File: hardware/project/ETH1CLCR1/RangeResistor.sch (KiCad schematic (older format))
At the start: 13 parts

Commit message: Schematic design
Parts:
- added C? (x5): C, symbol Device:C
- added C? (x2): 10p, symbol Device:C
- added C?: 2-8p, symbol Device:CTRIM
- added C?: 5-35p, symbol Device:CTRIM
- added C?: 1u, symbol Device:C
- added D? (x5): 1N4148, symbol Device:D
- added D? (x2): D, symbol Device:D
- added J? (x2): Conn_Coaxial, symbol Connector:Conn_Coaxial
- added K?: TQ2SA-5V, symbol ETH1CLCR1:TQ2SA-5V
- added Q? (x2): BC847W, Package_TO_SOT_SMD:SOT-323_SC-70, symbol Transistor_BJT:BC847W
- added Q?: 2N2218A, symbol Device:Q_NPN_BEC
- added Q?: 2N2904A, symbol Device:Q_PNP_BEC
- added R? (x20): R, symbol Device:R
- added R?: 10, symbol Device:R
- added R?: 100, symbol Device:R
- added R?: 1k01, symbol Device:R
- added R? (x6): 10k, symbol Device:R
- added R? (x2): 47, symbol Device:R
- added R? (x2): 51R1, symbol Device:R
- added R? (x2): 2R7/2W, symbol Device:R
- added R? (x2): 261, symbol Device:R
- added R?: 90k, symbol Device:R
- added RV?: 500, symbol Device:R_POT_TRIM
- added U? (x12): TLP3542, Package_DIP:DIP-5-6_W7.62mm, symbol Relay_SolidState:TLP3542
- added U?: HA3-2525-5Z, symbol ETH1CLCR1:HA3-2525-5Z
- added U? (x3): RC4558, symbol Amplifier_Operational:RC4558
- added U?: AD5293BRUZ-20, Package_SO:TSSOP-14_4.4x5mm_P0.65mm, symbol Potentiometer_Digital:AD5293
- D? (x4): value D_Small -> 1N4148
- R?: value R -> 100
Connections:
- net labels added: +15VF, +3.3VP, +5VF, -15VF, 100KNPN, Err, Lc, Lp, R100CRT, R100KCRT, R10CRT, R10KCRT, R1KCRT
- wire segments 37 -> 241
- no-connect marks 0 -> 4
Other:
- note removed: "Protection circuit"
- moved on the sheet: C?, D?, R?

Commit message: Schematic design
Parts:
- gave numbers to parts that had none: 91
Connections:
- net labels added: +12VF, -12VF

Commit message: Schematic design
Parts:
- removed D1305, D1306: D_Small, symbol Device:D_Small
- removed J1301, J1302: Conn_Coaxial, symbol Connector:Conn_Coaxial
- removed U1302, U1305, U1306, U1307, U1308, U1309, U1310, U1311, U1312, U1313, U1314, U1315: TLP3542, Package_DIP:DIP-5-6_W7.62mm, symbol Relay_SolidState:TLP3542
- added D1305: BAT54SW, Package_TO_SOT_SMD:SOT-323_SC-70, symbol Diode:BAT54SW
- added RV1302: 20k, Resistor_SMD:R_0603_1608Metric_Pad1.05x0.95mm_HandSolder, symbol Device:R_POT_TRIM
- added U1302, U1305, U1306, U1307, U1308, U1309, U1310, U1311, U1312, U1313, U1314, U1315: AQY212GS, symbol ETH1CLCR1:AQY212GS
- C1302, C1303, C1311, C1312: footprint (none) -> Capacitor_SMD:C_0603_1608Metric_Pad1.05x0.95mm_HandSolder
- C1304: value C -> 1u
- C1305: value C -> 47p; footprint (none) -> Capacitor_SMD:C_0603_1608Metric_Pad1.05x0.95mm_HandSolder
- C1307: value C -> 33p; footprint (none) -> Capacitor_SMD:C_0603_1608Metric_Pad1.05x0.95mm_HandSolder
- C1308: value C -> 6800p; footprint (none) -> Capacitor_SMD:C_0603_1608Metric_Pad1.05x0.95mm_HandSolder
- C1309: value C -> 39p; footprint (none) -> Capacitor_SMD:C_0603_1608Metric_Pad1.05x0.95mm_HandSolder
- D1307, D1308: value D -> 1N4148
- R1302: value R -> 1k
- R1303, R1304, R1305, R1306, R1309, R1310, R1311, R1314, R1315, R1316, R1317, R1319, R1322, R1323, R1325, R1326, R1327, R1329, R1340, R1343, RV1301: footprint (none) -> Resistor_SMD:R_0603_1608Metric_Pad1.05x0.95mm_HandSolder
- R1307, R1330, R1331, R1332, R1333, R1334, R1335, R1336, R1337, R1339, R1341, R1342: value R -> 330; footprint (none) -> Resistor_SMD:R_0603_1608Metric_Pad1.05x0.95mm_HandSolder
- R1308: value R -> 550; footprint (none) -> Resistor_SMD:R_0603_1608Metric_Pad1.05x0.95mm_HandSolder
- R1312, R1324: value R -> 10k; footprint (none) -> Resistor_SMD:R_0603_1608Metric_Pad1.05x0.95mm_HandSolder
- R1313: value R -> 5M6; footprint (none) -> Resistor_SMD:R_0603_1608Metric_Pad1.05x0.95mm_HandSolder
- R1318: value R -> 3k3; footprint (none) -> Resistor_SMD:R_0603_1608Metric_Pad1.05x0.95mm_HandSolder
- R1328: value R -> 1k111; footprint (none) -> Resistor_SMD:R_0603_1608Metric_Pad1.05x0.95mm_HandSolder
- R1338: value R -> 13R3; footprint (none) -> Resistor_SMD:R_0603_1608Metric_Pad1.05x0.95mm_HandSolder
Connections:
- net labels added: +3.3VF, HA3-COMP, HPOT, LCUR, LPOT, RELAY_CTR, RR_CLK, RR_OFFS1, RR_RDY, RR_SDI, RR_SDO, RR_~CS, RR_~RST
- net labels removed: +3.3VP, Lc, Lp
- wire segments 241 -> 242
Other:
- moved on the sheet: C1312, Q1304, R1305, R1343, U1304C

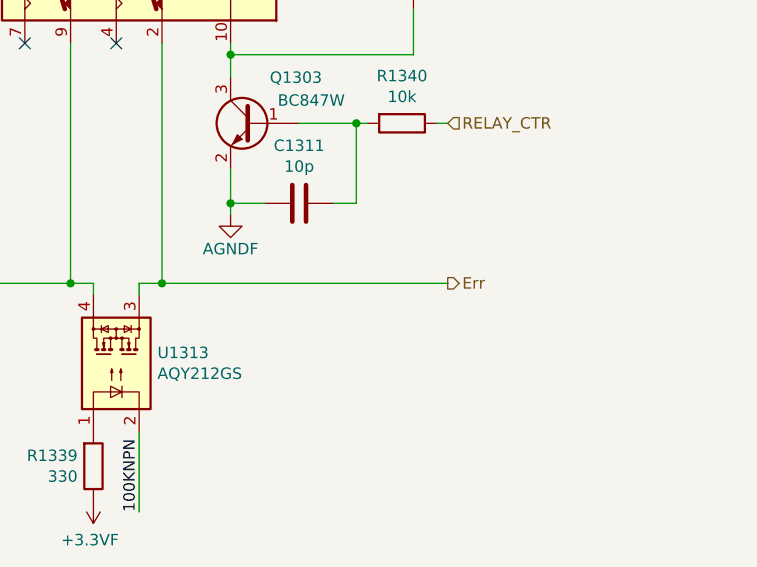
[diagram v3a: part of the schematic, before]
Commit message: Need to redesign the AC source, the LT1468 is too slow.
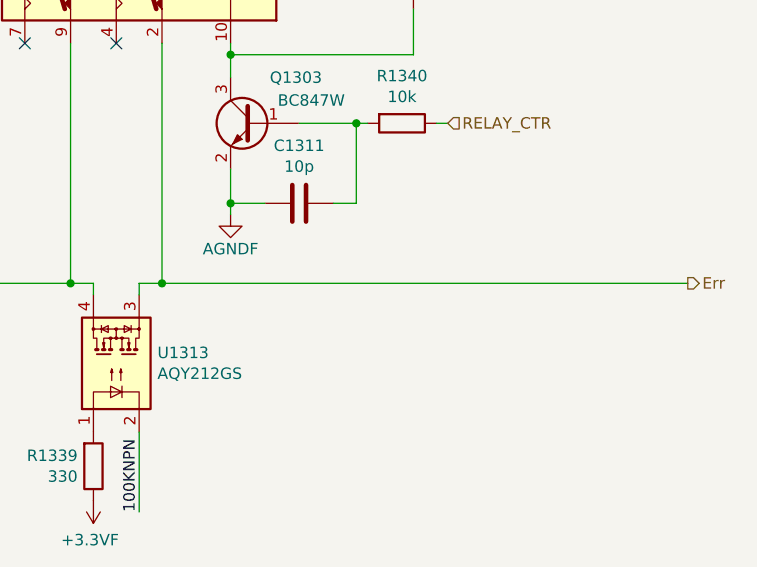
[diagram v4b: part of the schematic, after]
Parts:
- D1301, D1302, D1303, D1304, D1307, D1308, D1309, D1310, D1311, D1312, D1313: footprint (none) -> Diode_SMD:D_SOD-123
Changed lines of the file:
@@
 F 0 "D1313" V 13104 6579 50  0000 L CNN
 F 1 "1N4148" V 13195 6579 50  0000 L CNN
-F 2 "" H 13150 6500 50  0001 C CNN
+F 2 "Diode_SMD:D_SOD-123" H 13150 6500 50  0001 C CNN
 F 3 "~" H 13150 6500 50  0001 C CNN
 	1    13150 6500
@@
 Connection ~ 11650 7850
 Wire Wire Line
-	12050 7850 13300 7850
+	12050 7850 14350 7850
 Connection ~ 12050 7850
-Text HLabel 13300 7850 2    50   Output ~ 0
+Text HLabel 14350 7850 2    50   Output ~ 0
 Err
 $Comp
@@
 F 0 "D1310" H 7900 8034 50  0000 C CNN
 F 1 "1N4148" H 7900 8125 50  0000 C CNN
-F 2 "" H 7900 8250 50  0001 C CNN
+F 2 "Diode_SMD:D_SOD-123" H 7900 8250 50  0001 C CNN
 F 3 "~" H 7900 8250 50  0001 C CNN
 	1    7900 8250
@@
 F 0 "D1309" H 7900 7666 50  0000 C CNN
 F 1 "1N4148" H 7900 7575 50  0000 C CNN
-F 2 "" H 7900 7450 50  0001 C CNN
+F 2 "Diode_SMD:D_SOD-123" H 7900 7450 50  0001 C CNN
 F 3 "~" H 7900 7450 50  0001 C CNN
 	1    7900 7450
@@
 F 0 "D1308" V 7346 8271 50  0000 R CNN
 F 1 "1N4148" V 7255 8271 50  0000 R CNN
-F 2 "" H 7300 8350 50  0001 C CNN
+F 2 "Diode_SMD:D_SOD-123" H 7300 8350 50  0001 C CNN
 F 3 "~" H 7300 8350 50  0001 C CNN
 	1    7300 8350
@@
 F 0 "D1307" V 7346 7271 50  0000 R CNN
 F 1 "1N4148" V 7255 7271 50  0000 R CNN
-F 2 "" H 7300 7350 50  0001 C CNN
+F 2 "Diode_SMD:D_SOD-123" H 7300 7350 50  0001 C CNN
 F 3 "~" H 7300 7350 50  0001 C CNN
 	1    7300 7350
@@
 F 0 "D1304" V 3596 7532 50  0000 R CNN
 F 1 "1N4148" V 3505 7532 50  0000 R CNN
-F 2 "" V 3550 7600 50  0001 C CNN
+F 2 "Diode_SMD:D_SOD-123" V 3550 7600 50  0001 C CNN
 F 3 "~" V 3550 7600 50  0001 C CNN
 	1    3550 7600
@@
 F 0 "D1302" V 3004 7668 50  0000 L CNN
 F 1 "1N4148" V 3095 7668 50  0000 L CNN
-F 2 "" V 3050 7600 50  0001 C CNN
+F 2 "Diode_SMD:D_SOD-123" V 3050 7600 50  0001 C CNN
 F 3 "~" V 3050 7600 50  0001 C CNN
 	1    3050 7600
@@
 F 0 "D1303" V 3596 6432 50  0000 R CNN
 F 1 "1N4148" V 3505 6432 50  0000 R CNN
-F 2 "" V 3550 6500 50  0001 C CNN
+F 2 "Diode_SMD:D_SOD-123" V 3550 6500 50  0001 C CNN
 F 3 "~" V 3550 6500 50  0001 C CNN
 	1    3550 6500
@@
 F 0 "D1301" V 3004 6568 50  0000 L CNN
 F 1 "1N4148" V 3095 6568 50  0000 L CNN
-F 2 "" V 3050 6500 50  0001 C CNN
+F 2 "Diode_SMD:D_SOD-123" V 3050 6500 50  0001 C CNN
 F 3 "~" V 3050 6500 50  0001 C CNN
 	1    3050 6500
@@
 F 0 "D1311" H 8300 7666 50  0000 C CNN
 F 1 "1N4148" H 8300 7575 50  0000 C CNN
-F 2 "" H 8300 7450 50  0001 C CNN
+F 2 "Diode_SMD:D_SOD-123" H 8300 7450 50  0001 C CNN
 F 3 "~" H 8300 7450 50  0001 C CNN
 	1    8300 7450
@@
 F 0 "D1312" H 8300 8034 50  0000 C CNN
 F 1 "1N4148" H 8300 8125 50  0000 C CNN
-F 2 "" H 8300 8250 50  0001 C CNN
+F 2 "Diode_SMD:D_SOD-123" H 8300 8250 50  0001 C CNN
 F 3 "~" H 8300 8250 50  0001 C CNN
 	1    8300 8250

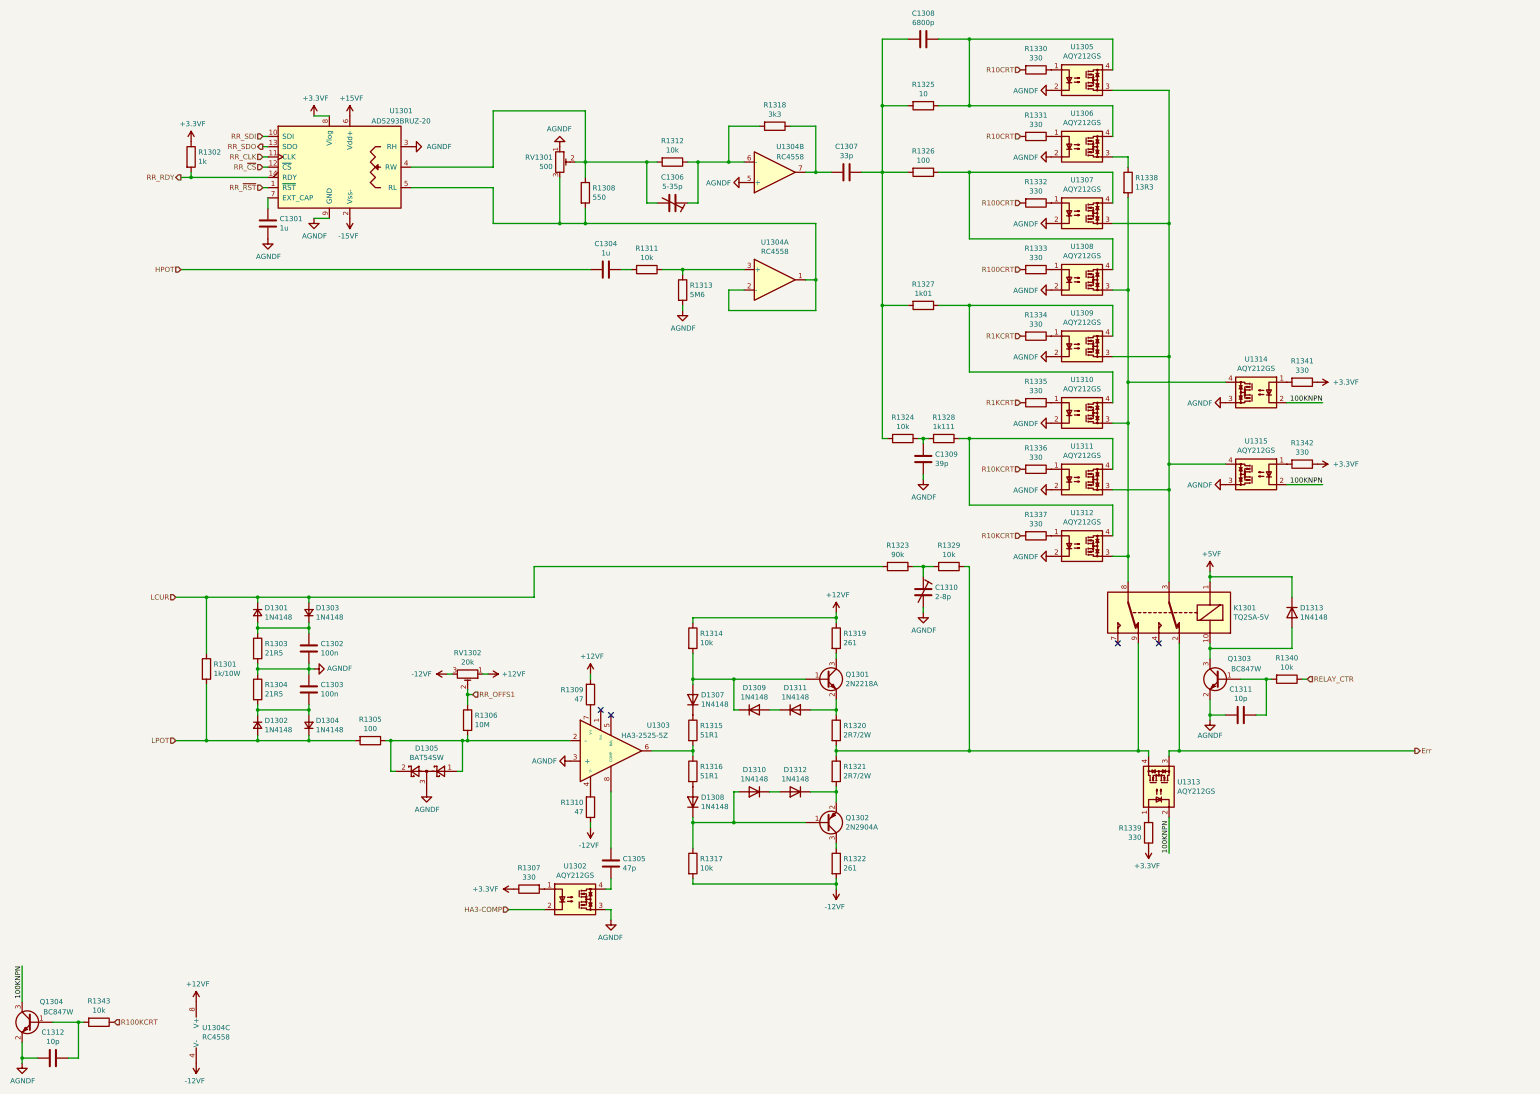
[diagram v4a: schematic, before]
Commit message: Footprint asigment (not finished).
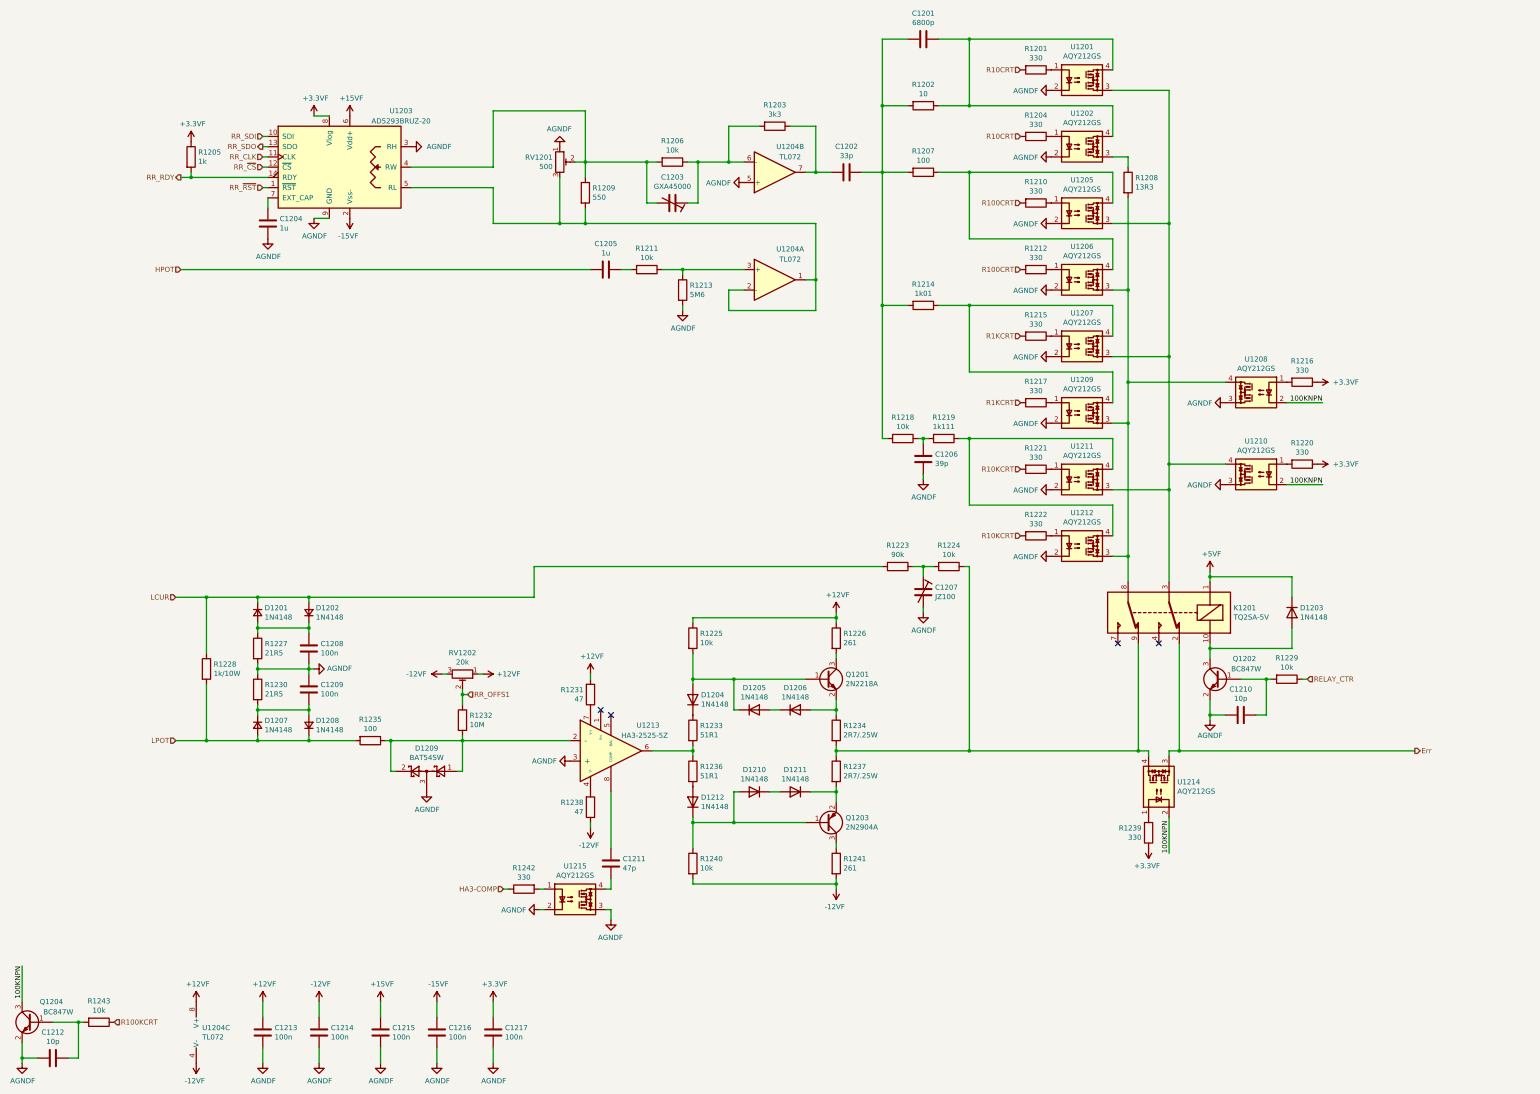
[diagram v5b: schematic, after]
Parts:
- removed U1304: RC4558, symbol Amplifier_Operational:RC4558
- added C1213, C1214, C1215, C1216, C1217: 100n, Capacitor_SMD:C_0603_1608Metric_Pad1.05x0.95mm_HandSolder, symbol Device:C
- added U1204: TL072, Package_SO:SOIC-8_3.9x4.9mm_P1.27mm, symbol Amplifier_Operational:TL072
- C1203: renamed from C1306; value 5-35p -> GXA45000
- C1204: renamed from C1301; footprint (none) -> Capacitor_SMD:C_0805_2012Metric_Pad1.15x1.40mm_HandSolder
- C1205: renamed from C1304; footprint (none) -> Capacitor_SMD:C_0805_2012Metric_Pad1.15x1.40mm_HandSolder
- C1207: renamed from C1310; value 2-8p -> JZ100
- K1201: renamed from K1301; footprint (none) -> ETH1CLCR1:SA
- Q1201: renamed from Q1301; footprint (none) -> Package_TO_SOT_THT:TO-39-3
- Q1203: renamed from Q1302; footprint (none) -> Package_TO_SOT_THT:TO-39-3
- R1205: renamed from R1302; footprint (none) -> Resistor_SMD:R_0603_1608Metric_Pad1.05x0.95mm_HandSolder
- R1234: renamed from R1320; value 2R7/2W -> 2R7/.25W
- R1237: renamed from R1321; value 2R7/2W -> 2R7/.25W
- U1201: renamed from U1305; footprint (none) -> ETH1CLCR1:AQY212GS
- U1202: renamed from U1306; footprint (none) -> ETH1CLCR1:AQY212GS
- U1205: renamed from U1307; footprint (none) -> ETH1CLCR1:AQY212GS
- U1206: renamed from U1308; footprint (none) -> ETH1CLCR1:AQY212GS
- U1207: renamed from U1309; footprint (none) -> ETH1CLCR1:AQY212GS
- U1208: renamed from U1314; footprint (none) -> ETH1CLCR1:AQY212GS
- U1209: renamed from U1310; footprint (none) -> ETH1CLCR1:AQY212GS
- U1210: renamed from U1315; footprint (none) -> ETH1CLCR1:AQY212GS
- U1211: renamed from U1311; footprint (none) -> ETH1CLCR1:AQY212GS
- U1212: renamed from U1312; footprint (none) -> ETH1CLCR1:AQY212GS
- U1213: renamed from U1303; footprint (none) -> Package_DIP:DIP-8_W10.16mm_LongPads
- U1214: renamed from U1313; footprint (none) -> ETH1CLCR1:AQY212GS
- U1215: renamed from U1302; footprint (none) -> ETH1CLCR1:AQY212GS
- renumbered C1308 to C1201, C1307 to C1202, C1309 to C1206, C1302 to C1208, C1303 to C1209, C1311 to C1210, C1305 to C1211, C1312 to C1212, D1301 to D1201, D1303 to D1202, D1313 to D1203, D1307 to D1204, D1309 to D1205, D1311 to D1206, D1302 to D1207, D1304 to D1208, D1305 to D1209, D1310 to D1210, D1312 to D1211, D1308 to D1212, Q1303 to Q1202, Q1304 to Q1204, R1330 to R1201, R1325 to R1202, R1318 to R1203, R1331 to R1204, R1312 to R1206, R1326 to R1207, R1338 to R1208, R1308 to R1209, R1332 to R1210, R1311 to R1211, R1333 to R1212, R1313 to R1213, R1327 to R1214, R1334 to R1215, R1341 to R1216, R1335 to R1217, R1324 to R1218, R1328 to R1219, R1342 to R1220, R1336 to R1221, R1337 to R1222, R1323 to R1223, R1329 to R1224, R1314 to R1225, R1319 to R1226, R1303 to R1227, R1301 to R1228, R1340 to R1229, R1304 to R1230, R1309 to R1231, R1306 to R1232, R1315 to R1233, R1305 to R1235, R1316 to R1236, R1310 to R1238, R1339 to R1239, R1317 to R1240, R1322 to R1241, R1307 to R1242, R1343 to R1243, RV1301 to RV1201, RV1302 to RV1202, U1301 to U1203
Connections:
- net +12VF: now also C1213.1, U1204.8 (V+)
- net +15VF: now also C1215.1
- net +3.3VF: now also C1217.1; no longer R1242.1
- net -12VF: now also C1214.1, U1204.4 (V-)
- net -15VF: now also C1216.1
- net AGNDF: now also U1215.2, C1213.2, C1214.2, C1215.2, C1216.2, C1217.2, U1204.5 (+)
- net HA3-COMP: now also R1242.1; no longer U1215.2
- net at C1202.2, R1203.1: now also U1204.7
- net at R1209.2, RV1201.3, U1203.5 (RL): now also U1204.1, U1204.2 (-)
- net at R1211.1, R1213.1: now also U1204.3 (+)
- net at C1203.1, R1203.2, R1206.1: now also U1204.6 (-)
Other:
- moved on the sheet: R1232, R1242, RV1202

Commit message: Modification in schematic and PCB layout.
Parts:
- C1203: value GXA45000 -> BFC280908002; footprint (none) -> ETH1CLCR1:BFC2
- C1204, C1205: footprint Capacitor_SMD:C_0805_2012Metric_Pad1.15x1.40mm_HandSolder -> Capacitor_SMD:C_0603_1608Metric_Pad1.05x0.95mm_HandSolder
- C1207: footprint (none) -> ETH1CLCR1:JZ
- R1228: value 1k/10W -> 1k/.25W; footprint (none) -> Resistor_SMD:R_1206_3216Metric_Pad1.42x1.75mm_HandSolder
- R1234, R1237: footprint (none) -> Resistor_SMD:R_0805_2012Metric_Pad1.15x1.40mm_HandSolder
- RV1201: value 500 -> 3314J-1-501E; footprint Resistor_SMD:R_0603_1608Metric_Pad1.05x0.95mm_HandSolder -> Potentiometer_SMD:Potentiometer_Bourns_3314J_Vertical
- RV1202: value 20k -> 3314J-1-203E; footprint Resistor_SMD:R_0603_1608Metric_Pad1.05x0.95mm_HandSolder -> Potentiometer_SMD:Potentiometer_Bourns_3314J_Vertical
- U1213: footprint Package_DIP:DIP-8_W10.16mm_LongPads -> Package_DIP:DIP-8_W7.62mm
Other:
- moved on the sheet: C1201, C1202, C1203, C1204, C1205, C1206, C1207, C1208, C1209, C1210, C1211, C1213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
